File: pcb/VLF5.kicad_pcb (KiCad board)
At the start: 6 copper layers, 34 x 56 mm, 105 parts, among them CN1 532610571, J1 Conn_01x02_Pin, Q1 SS8050, Q3 SS8050, Q4 SS8050, Q5 SI7232DN-T1-GE3, U1 STM32H743VIHx, U10 LSM6DSMTR, U11 LIS2MDL, U12 BWU.FL-IPEX1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

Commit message: Saving for Edits
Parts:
- moved C29 38.0 mm to (99.2, 45.3)
- moved C39 38.0 mm to (99.7, 52.1)
- moved C44 38.0 mm to (99.7, 50.2)
- moved U1 38.0 mm to (105.2, 49.1)
- moved X1 38.0 mm to (98.7, 47.5)
- moved C30 38.0 mm to (98.1, 49.8)
- moved C36 38.0 mm to (101.1, 54.6)
- moved RBOOT1 19.7 mm to (105.2, 44.2)
- moved C38 16.8 mm to (102.1, 46.9)
- moved C31 15.8 mm to (104.8, 49.4), turned to -90 degrees
- moved C40 15.4 mm to (105.8, 49.4)
- moved C35 14.3 mm to (107.8, 50.5)
- moved C34 14.2 mm to (106.8, 48.6), turned to -90 degrees
- moved C32 13.9 mm to (102.4, 48.3), turned to 0 degrees
- moved C33 13.7 mm to (103.8, 49.4)
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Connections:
- J1 pad S2: (no net) -> +BATT
- J_PYRO1 pad S1: (no net) -> Net-(J_PYRO1-Pin_3)
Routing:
- net /LORA_nRST: track 12.6 -> 15.4 mm
- net Net-(U1-BOOT0): track 0.57 -> 3.36 mm, vias 0 -> 1
- net GND: track 11.5 -> 13.1 mm
- net Net-(C35-Pad2): track 0.57 -> 0.00 mm
- net +3.3V: track 12.0 -> 12.6 mm, vias 6 -> 7

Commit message: Potential Layout 1
- LDO in place?
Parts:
- moved C29 37.7 mm to (64.2, 59.3)
- moved C31 37.7 mm to (69.8, 63.4)
- moved C32 37.7 mm to (67.4, 62.3)
- moved C33 37.7 mm to (68.8, 63.4)
- moved C34 37.7 mm to (71.8, 62.6)
- moved C35 37.7 mm to (72.8, 64.5)
- moved C37 37.7 mm to (71.8, 64.5)
- moved C38 37.7 mm to (67.1, 60.9)
- moved C40 37.7 mm to (70.8, 63.4)
- moved C44 37.7 mm to (64.7, 64.2)
- moved RBOOT1 37.7 mm to (70.2, 58.2)
- moved U1 37.7 mm to (70.2, 63.1)
- moved X1 37.7 mm to (63.7, 61.5)
- moved C30 37.7 mm to (63.1, 63.8)
- moved C36 37.7 mm to (66.1, 68.6)
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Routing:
- net Net-(J_CAN1-Pin_2): track 27.6 -> 0.00 mm, vias 1 -> 0
- net Net-(J_CAN1-Pin_1): track 26.9 -> 0.00 mm, vias 1 -> 0
- net Net-(J_CAN1-Pin_3): track 26.1 -> 0.00 mm, vias 1 -> 0
- net Net-(J_CAN1-Pin_4): track 25.5 -> 0.00 mm, vias 1 -> 0
- net /SWDCLK: track 20.8 -> 0.00 mm
- net /LORA_MOSI: track 18.8 -> 0.00 mm
- net /nRST: track 18.2 -> 0.00 mm, vias 2 -> 0
- net /LORA_MISO: track 17.3 -> 0.00 mm
- net /LORA_nRST: track 15.4 -> 0.00 mm
- net /LORA_BUSY: track 14.5 -> 0.00 mm
- net /LORA_TXEN: track 14.3 -> 0.00 mm
- net /LORA_RXEN: track 13.5 -> 0.00 mm
- net GND: track 13.1 -> 0.00 mm, vias 8 -> 0
- net +3.3V: track 12.6 -> 0.00 mm, vias 7 -> 0
- net /LORA_SCK: track 12.5 -> 0.00 mm
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
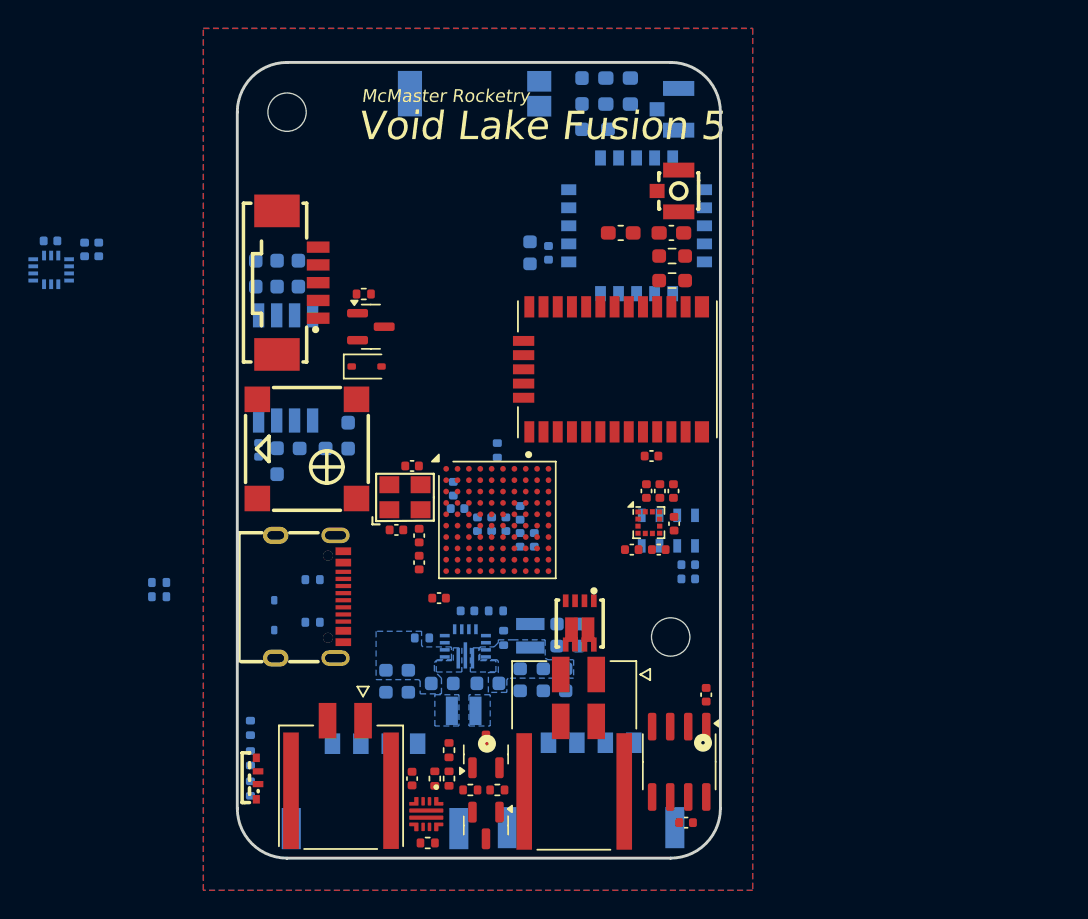
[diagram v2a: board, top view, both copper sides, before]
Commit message: More Progress
- Decoupling Capacitors Layed out
- GPIO pins changed around for GPS and LoRa
- STM Pin Vias Placed
WARNING: ALTERED NO-NET PADS KEEP RESETTING TO NO-NET ENSURE NO ERRORS IN DRC.
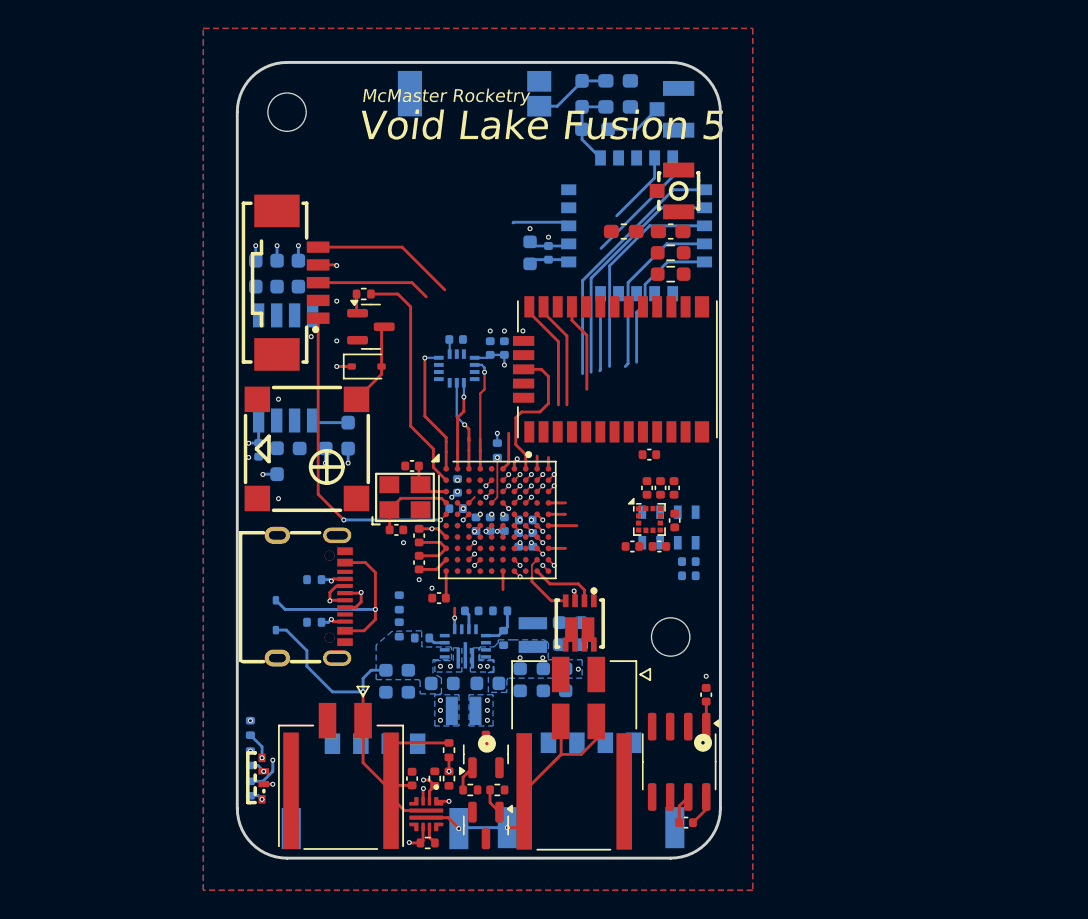
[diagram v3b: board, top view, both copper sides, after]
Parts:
- moved U10 29.4 mm to (67.3, 52.4)
- moved C16 29.4 mm to (70.7, 51.0)
- moved C17 29.4 mm to (69.7, 51.0)
- moved C18 29.4 mm to (67.3, 50.4)
- moved R12 17.1 mm to (63.3, 70.8), turned to 90 degrees
- moved R11 17.0 mm to (63.3, 68.9), turned to 90 degrees
- moved C34 0.64 mm to (72.2, 63.1), turned to 180 degrees
- moved R17 0.46 mm to (82.4, 45.8)
- moved LED2 0.40 mm to (53.7, 81.3)
- moved C38 0.36 mm to (67.4, 60.7)
- moved C5 0.30 mm to (68.4, 69.5)
- moved R6 0.30 mm to (70.4, 69.5)
- moved R16 0.25 mm to (82.4, 44.3)
- moved L3 0.24 mm to (79.1, 42.8)
- moved C22 0.22 mm to (82.7, 63.1)
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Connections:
- J1 pad S2: +BATT -> (no net)
- J_PYRO1 pad S1: Net-(J_PYRO1-Pin_3) -> (no net)
- U1 pad C7: /LORA_BUSY -> /GPS_nRST
- U1 pad D7: /LORA_CS -> /LORA_DIO1
- U1 pad D8: /LORA_RXEN -> /LORA_TXEN
- U1 pad D9: /LORA_DIO1 -> /LORA_RXEN
- U1 pad E10: /GPS_nRST -> /LORA_CS
- U1 pad E8: /LORA_TXEN -> /LORA_BUSY
- U1 pad K2: /LED_R_CTRL -> /LED_B_CTRL
- U1 pad K4: /LED_B_CTRL -> /LED_R_CTRL
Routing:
- net +BATT: track 0.00 -> 31.5 mm, vias 0 -> 1
- net +3.3V: track 0.00 -> 24.9 mm, vias 0 -> 20
- net /nRST: track 0.00 -> 22.3 mm, vias 0 -> 2
- net Net-(J_PYRO1-Pin_3): track 0.00 -> 20.9 mm, vias 0 -> 2
- net /LORA_MISO: track 0.00 -> 19.3 mm
- net /LORA_BUSY: track 0.00 -> 17.8 mm
- net /BUZZER_CTRL: track 0.00 -> 16.4 mm
- net /VBUS: track 0.00 -> 16.0 mm, vias 0 -> 2
- net /LORA_MOSI: track 0.00 -> 15.5 mm, vias 0 -> 1
- net /LORA_CS: track 0.00 -> 13.7 mm
- net GND: track 0.00 -> 11.7 mm, vias 0 -> 28
- net /LORA_SCK: track 0.00 -> 11.3 mm, vias 0 -> 1
- net /SWDCLK: track 0.00 -> 11.1 mm
- net /GPS_PPS: track 0.00 -> 10.5 mm
- net /IMU_INT1: track 0.00 -> 9.41 mm, vias 0 -> 1
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
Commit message: Committing Current Progress just in case
As title describes
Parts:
- moved R12 0.22 mm to (63.4, 71.0)
- moved R11 0.22 mm to (63.4, 69.1)
- moved C9 0.12 mm to (76.2, 71.1)
- moved C36 0.12 mm to (66.0, 68.6)
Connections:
- J1 pad S2: (no net) -> +BATT
- J_CAN1 pad 6: (no net) -> Net-(J_PYRO1-Pin_3)
- J_CAN2 pad 5: (no net) -> Net-(J_PYRO1-Pin_3)
- J_PYRO1 pad S1: (no net) -> Net-(J_PYRO1-Pin_3)
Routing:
- net GND: track 11.7 -> 9.58 mm, vias 28 -> 30
- net +3.3V: track 24.9 -> 25.6 mm, vias 20 -> 21
- net +3.3VA: vias 0 -> 3
- added copper zone on B.Cu, net +3.3VA
- added copper zone on In3.Cu, net Net-(U4-L1)
- added copper zone on In3.Cu, net Net-(U4-L2)

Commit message: More Routing
Saving in case
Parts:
- moved C42 2.17 mm to (83.5, 63.9)
- moved C43 2.17 mm to (81.6, 63.9)
- moved U11 2.14 mm to (82.8, 62.1)
- moved C22 2.06 mm to (84.6, 62.4)
- moved C23 1.39 mm to (82.7, 59.9)
- moved C24 1.39 mm to (81.8, 59.9)
- moved C41 1.39 mm to (83.7, 59.9)
- moved C30 1.10 mm to (62.0, 63.9), turned to 180 degrees
- moved C18 1.10 mm to (66.2, 50.4), turned to 180 degrees
- moved C11 1.05 mm to (83.7, 67.1), turned to 180 degrees
- moved U9 1.00 mm to (81.3, 63.6)
- moved RBOOT1 0.98 mm to (69.8, 57.3)
- moved C12 0.95 mm to (83.7, 66.1), turned to 180 degrees
- moved C9 0.93 mm to (76.7, 70.3), turned to 180 degrees
- moved C27 0.64 mm to (80.5, 59.0), turned to 90 degrees
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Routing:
- net Net-(J_CAN1-Pin_4): track 0.00 -> 31.8 mm, vias 0 -> 3
- net Net-(J_CAN1-Pin_1): track 2.19 -> 31.6 mm, vias 0 -> 2
- net Net-(J_CAN1-Pin_3): track 0.00 -> 28.4 mm, vias 0 -> 1
- net Net-(J_CAN1-Pin_2): track 2.07 -> 29.9 mm, vias 0 -> 3
- net /DP: track 3.69 -> 28.8 mm
- net /VBUS: track 16.0 -> 39.9 mm
- net /nRST: track 22.3 -> 0.57 mm
- net /DN: track 3.49 -> 24.7 mm
- net /Pyro/PYRO2: track 0.00 -> 15.5 mm, vias 0 -> 2
- net +3.3V: track 25.6 -> 40.8 mm, vias 21 -> 31
- net /Pyro/PYRO1: track 0.00 -> 14.3 mm, vias 0 -> 2
- net /LORA_MISO: track 19.3 -> 6.87 mm
- net Net-(J_PYRO1-Pin_3): track 20.9 -> 9.41 mm
- net /LORA_BUSY: track 17.8 -> 6.41 mm
- net /GPS_PPS: track 10.5 -> 2.84 mm
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- added copper zone on In3.Cu, net +3.3V
- added copper zone on In3.Cu, net +3.3VA
- removed copper zone on In3.Cu, net GND

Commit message: Playing with routing paths
almost there
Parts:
- moved RBOOT1 1.40 mm to (69.8, 55.9)
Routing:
- net /CAN_TX: track 0.00 -> 25.8 mm
- net /nRST: track 0.57 -> 22.3 mm
- net /CAN_RX: track 0.00 -> 20.1 mm
- net /LED_R_CTRL: track 3.66 -> 17.2 mm, vias 1 -> 2
- net /LED_G_CTRL: track 2.97 -> 16.1 mm, vias 1 -> 2
- net /LED_B_CTRL: track 2.61 -> 14.9 mm, vias 1 -> 2
- net /BARO_CLK: track 0.00 -> 11.9 mm
- net /IMU_MOSI: track 2.57 -> 10.9 mm, vias 1 -> 2
- net /BARO_MISO: track 0.00 -> 8.21 mm
- net /BAT_V_M: track 0.88 -> 8.32 mm
- net /LORA_MOSI: track 9.07 -> 15.3 mm, vias 0 -> 1
- net /IMU_INT1: track 3.81 -> 9.87 mm
- net Net-(U1-BOOT0): track 0.00 -> 5.81 mm
- net /SD_DAT2: track 2.11 -> 7.87 mm
- net /SD_DAT3: track 2.03 -> 7.31 mm
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
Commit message: About to change pins saving
oh boy
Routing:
- net /PYRO1_CONT: track 0.60 -> 28.6 mm
- net /SD_CLK: track 5.93 -> 31.9 mm, vias 1 -> 2
- net /SD_DAT0: track 5.26 -> 26.5 mm, vias 1 -> 2
- net /SD_DAT1: track 5.22 -> 26.3 mm, vias 1 -> 2
- net /SD_DAT2: track 7.87 -> 28.0 mm, vias 1 -> 2
- net /SD_DAT3: track 7.31 -> 26.2 mm, vias 1 -> 2
- net /PYRO_PG: track 1.57 -> 17.9 mm
- net /PYRO_nEN: track 2.82 -> 19.1 mm, vias 2 -> 3
- net /PYRO2_CONT: track 0.60 -> 16.4 mm, vias 2 -> 4
- net /LORA_MISO: track 10.1 -> 21.2 mm, vias 1 -> 2
- net /MAG_SCL: track 2.96 -> 13.9 mm, vias 1 -> 2
- net /BARO_MISO: track 8.21 -> 19.2 mm
- net /SD_CMD: track 5.35 -> 16.3 mm, vias 1 -> 2
- net /LORA_MOSI: track 15.3 -> 26.0 mm
- net /MAG_SDA: track 2.96 -> 13.2 mm, vias 1 -> 2
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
